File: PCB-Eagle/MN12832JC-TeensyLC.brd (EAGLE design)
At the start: 206.7 x 45.7 mm, 46 parts, among them IC4 ZXBM5210, IC6 74HC132D, SW3 EC12E_SW, SW4 EC12E_SW

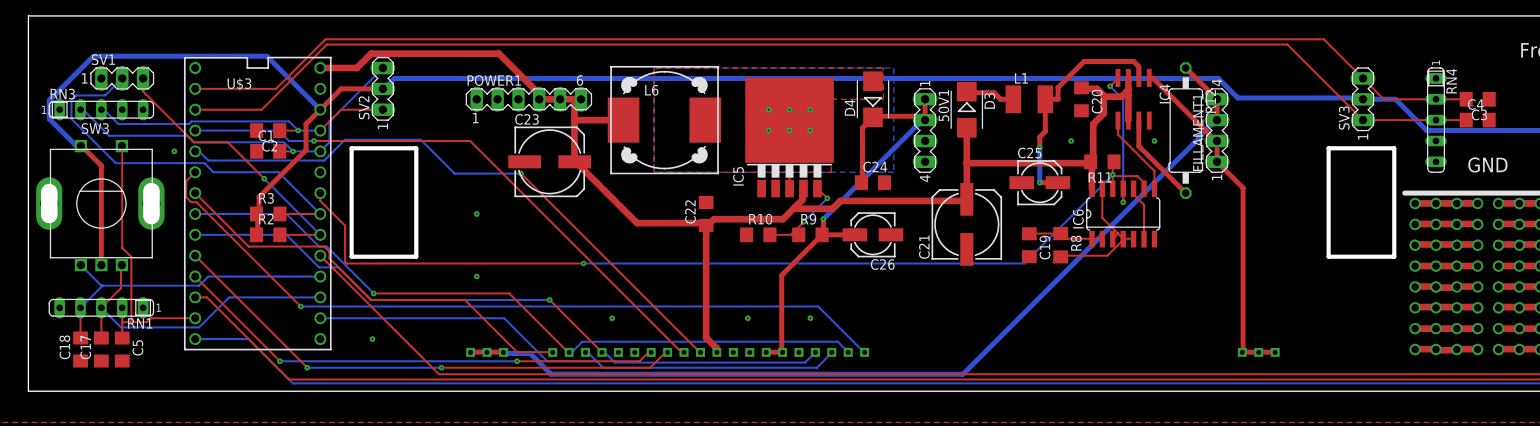
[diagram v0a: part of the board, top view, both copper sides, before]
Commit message: Larger Drills for Display
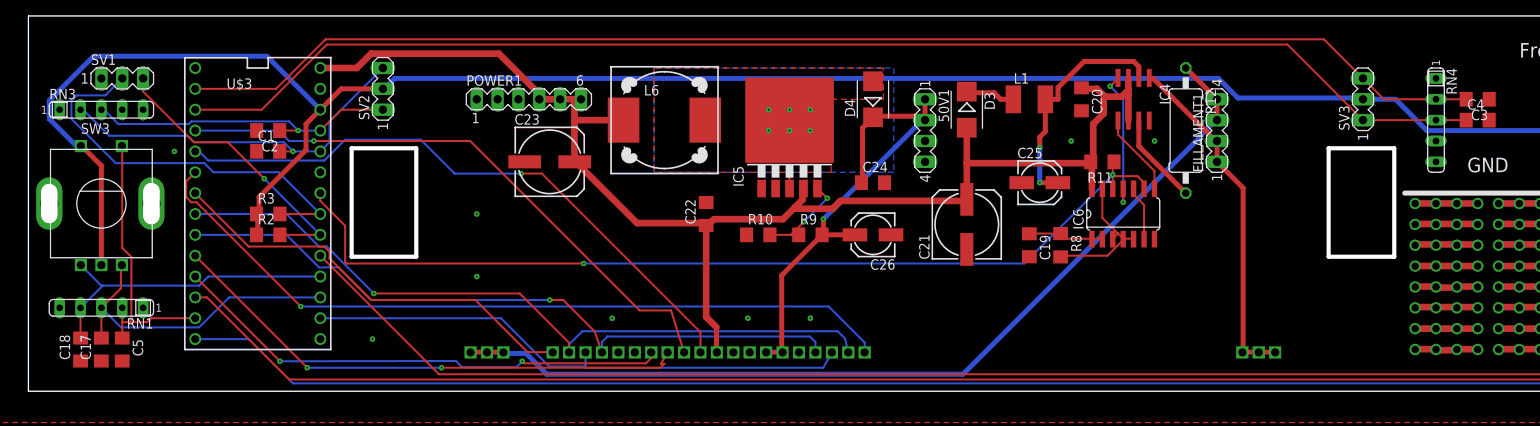
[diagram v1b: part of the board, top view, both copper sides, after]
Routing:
- net LAT12: track 87.6 -> 90.5 mm
- net MOSI: track 82.5 -> 85.3 mm
- net GLAT: track 70.7 -> 72.4 mm
- net GBLK: track 73.8 -> 75.2 mm
- net GSIN: track 60.3 -> 61.5 mm
- net GCLK: track 64.0 -> 65.0 mm
- net BLK1: track 94.0 -> 94.7 mm
